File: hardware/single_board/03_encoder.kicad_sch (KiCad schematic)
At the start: 2 parts, among them U10 MT6701

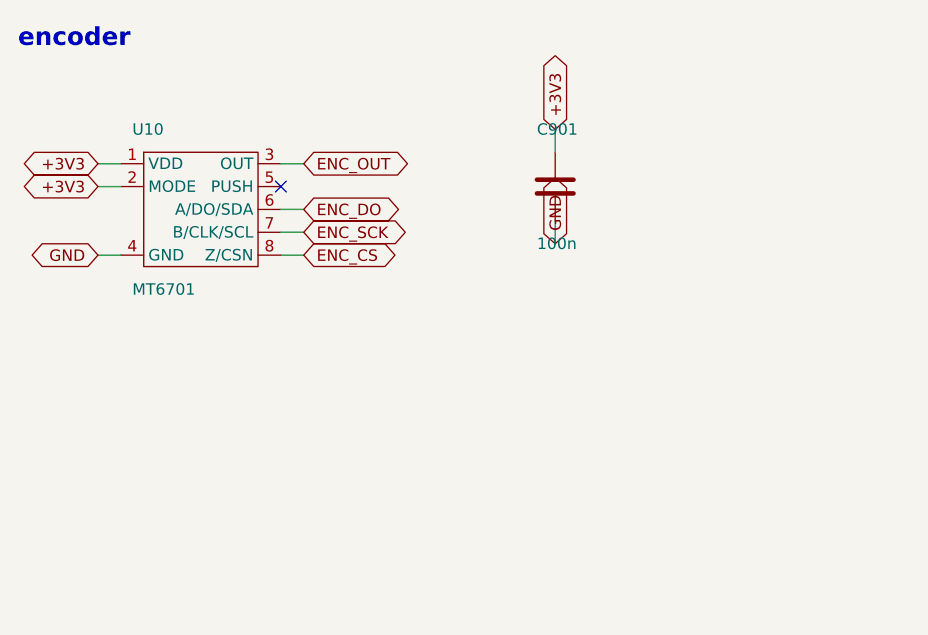
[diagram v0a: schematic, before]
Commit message: Board S schematic: drawn as a person would draw it, and on the page
The sheets were a grid of parts with a stub and a label on every pin.
tools/schdraw.py now draws a netlist from a hand-written layout: parts
placed and turned, wires between the pins that belong together, T-joins
split with a junction dot, ground and supply symbols on power pins, labels
only where a signal leaves its block. tools/schlayout_s.py is board S's
five sheets: signal left to right, supplies up, ground down, each part's
support parts at the pin they serve, dashed frames and notes. The header
pins and the notes follow the netlist, so a pin-map change redraws itself.

The drawing cannot change the circuit: every sheet is checked against
schematic_s's netlist before it is written, and `schdraw.py --check s`
compares KiCad's own netlist export net by net. It matches; ERC is 0 at
every severity; PCB parity is unchanged (the same 219 reports as before).

Found on the way: a symbol's instance path must be /<root>/<sheet>. With
the root left out, as schematic.py writes it, KiCad joins labelled nets
but silently drops every net that is only wire -- the old sheets labelled
every pin, so it never showed. Board A's generator is unchanged.

single.html: an SCH tab in the viewer (sch.js) -- the sheets as KiCad
plots them, a sheet list, drag to pan, scroll to zoom, a PDF of the lot.
tools/regen.py plots them into img/sch/s/ (--sch for that alone).

Co-Authored-By: Claude Opus 5.5 (1M context) <noreply@anthropic.com>
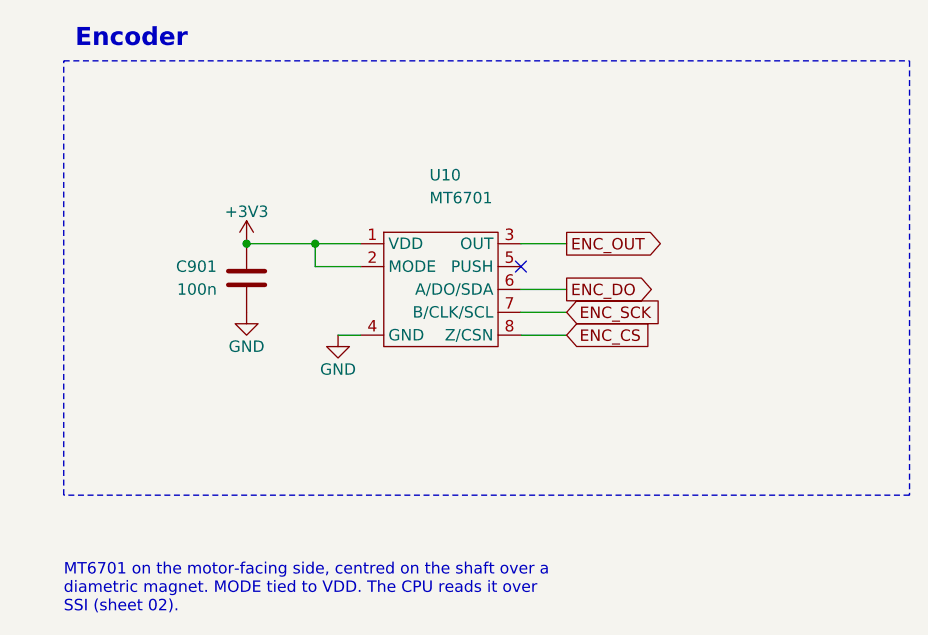
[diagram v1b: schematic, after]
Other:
- note added: "Encoder"
- note added: "MT6701 on the motor-facing side, centred on the shaft over a diametric magnet. MODE tied to VDD. The CPU reads it over SSI (sheet 02)."
- note removed: "encoder"
- moved on the sheet: C901, U10
